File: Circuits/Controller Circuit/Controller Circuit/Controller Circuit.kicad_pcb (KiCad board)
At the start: 2 copper layers, 124 x 95.8 mm, 12 parts, among them J1 Joystick, SW5 SW_Push, SW6 SW_Push, SW7 SW_Push, SW8 SW_Push, U1 ER_OLEDM0.91_1x-I2C, U2 NRF24L01_Breakout

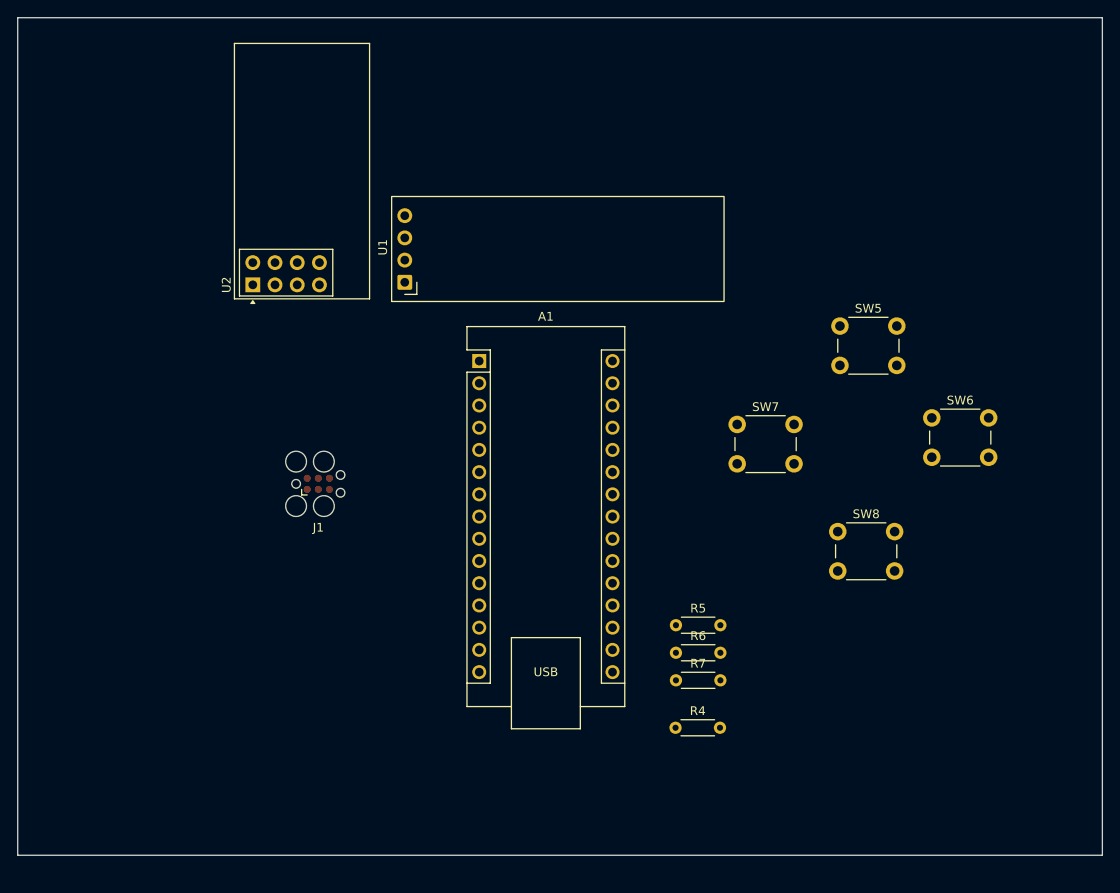
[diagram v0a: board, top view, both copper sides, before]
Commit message: Add regulators and boosters to schematics and footprints for other parts
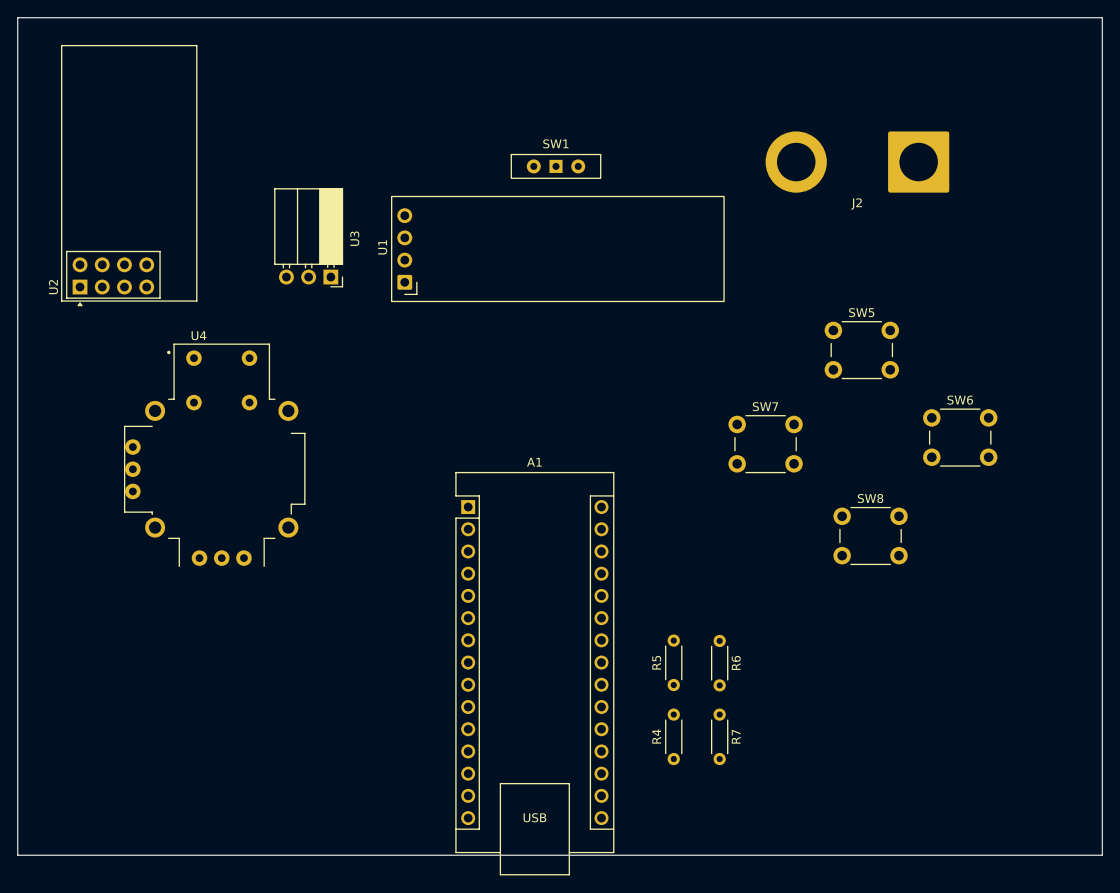
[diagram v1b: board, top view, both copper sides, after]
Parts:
- removed J1: Joystick, Connector:Tag-Connect_TC2030-IDC-FP_2x03_P1.27mm_Vertical
- added J2: Battery, Connector_Wire:SolderWire-6sqmm_1x02_P14mm_D3.5mm_OD7mm, F.Cu at (174.5, 58.0)
- added SW1: SW_SPDT, Button_Switch_THT:SW_Slide-03_Wuerth-WS-SLTV_10x2.5x6.4_P2.54mm, F.Cu at (133.0, 58.5)
- added U3: AMS1117-3.3, Connector_PinSocket_2.54mm:PinSocket_1x03_P2.54mm_Horizontal, F.Cu at (107.3, 71.2)
- added U4: Joystick, Custom Parts:XDCR_COM-09032, F.Cu at (94.8, 93.1)
- U1: value ER_OLEDM0.91_1x-I2C -> OLED
- moved U2 19.8 mm to (78.6, 72.3)
- moved A1 16.7 mm to (123.0, 97.4)
- moved R5 6.84 mm to (146.5, 117.8), turned to 90 degrees
- moved R7 6.35 mm to (151.8, 121.2), turned to -90 degrees
- moved R6 5.18 mm to (151.8, 112.8), turned to -90 degrees
- moved R4 3.58 mm to (146.5, 126.2), turned to 90 degrees
- moved SW8 1.82 mm to (165.8, 98.5)
- moved SW5 0.90 mm to (164.8, 77.2)
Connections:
- net Net-(A1-SCL/A5) renamed /OLED SCL
- net Net-(A1-SDA/A4) renamed /OLED SDA
- A1 pad 27: Net-(A1-VUSB/5V) -> unconnected-(A1-VUSB/5V-Pad27)
- A1 pad 30: unconnected-(A1-VIN-Pad30) -> /VOUT +
- SW5 pad 1: +5V -> Net-(J1-Pin_2)
- SW6 pad 1: +5V -> Net-(J1-Pin_2)
- SW7 pad 1: +5V -> Net-(J1-Pin_2)
- SW8 pad 1: +5V -> Net-(J1-Pin_2)
- U1 pad 2: Net-(A1-VUSB/5V) -> Net-(J1-Pin_2)
- U2 pad 2: +3.3V -> Net-(J1-Pin_2)
